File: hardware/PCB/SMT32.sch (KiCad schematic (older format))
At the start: 25 parts, among them J1 USB_B_Micro, SW1 SW_DIP_x01, SW2 SW_DIP_x01, U3 AZ1117CH-3.3, U4 STM32F303CCTx, Y1 X50328MSB2GI

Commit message: Use the correct Footprint
I think I can't do more things before the parts arrive and figure out what LED im going to use
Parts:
- removed U3: AZ1117CH-3.3, Package_TO_SOT_SMD:SOT-223-3_TabPin2, symbol Regulator_Linear:LD1117S33TR_SOT223
- added R14: 100k, Resistor_SMD:R_0402_1005Metric, symbol Device:R
- added U3: AZ1117-3.3, Package_TO_SOT_SMD:SOT-223-3_TabPin2, symbol Regulator_Linear:AZ1117-3.3
- renumbered C18 to C15, C17 to C16, C19 to C17, C20 to C18, C1 to C19, C22 to C20, C26 to C21, C23 to C22, C24 to C23, C25 to C24, R12 to R10, R13 to R11, R14 to R12, R15 to R13, R16 to R15, R17 to R16, R18 to R17, R19 to R18, R11 to R9
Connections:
- wire segments 65 -> 67
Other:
- moved on the sheet: R16

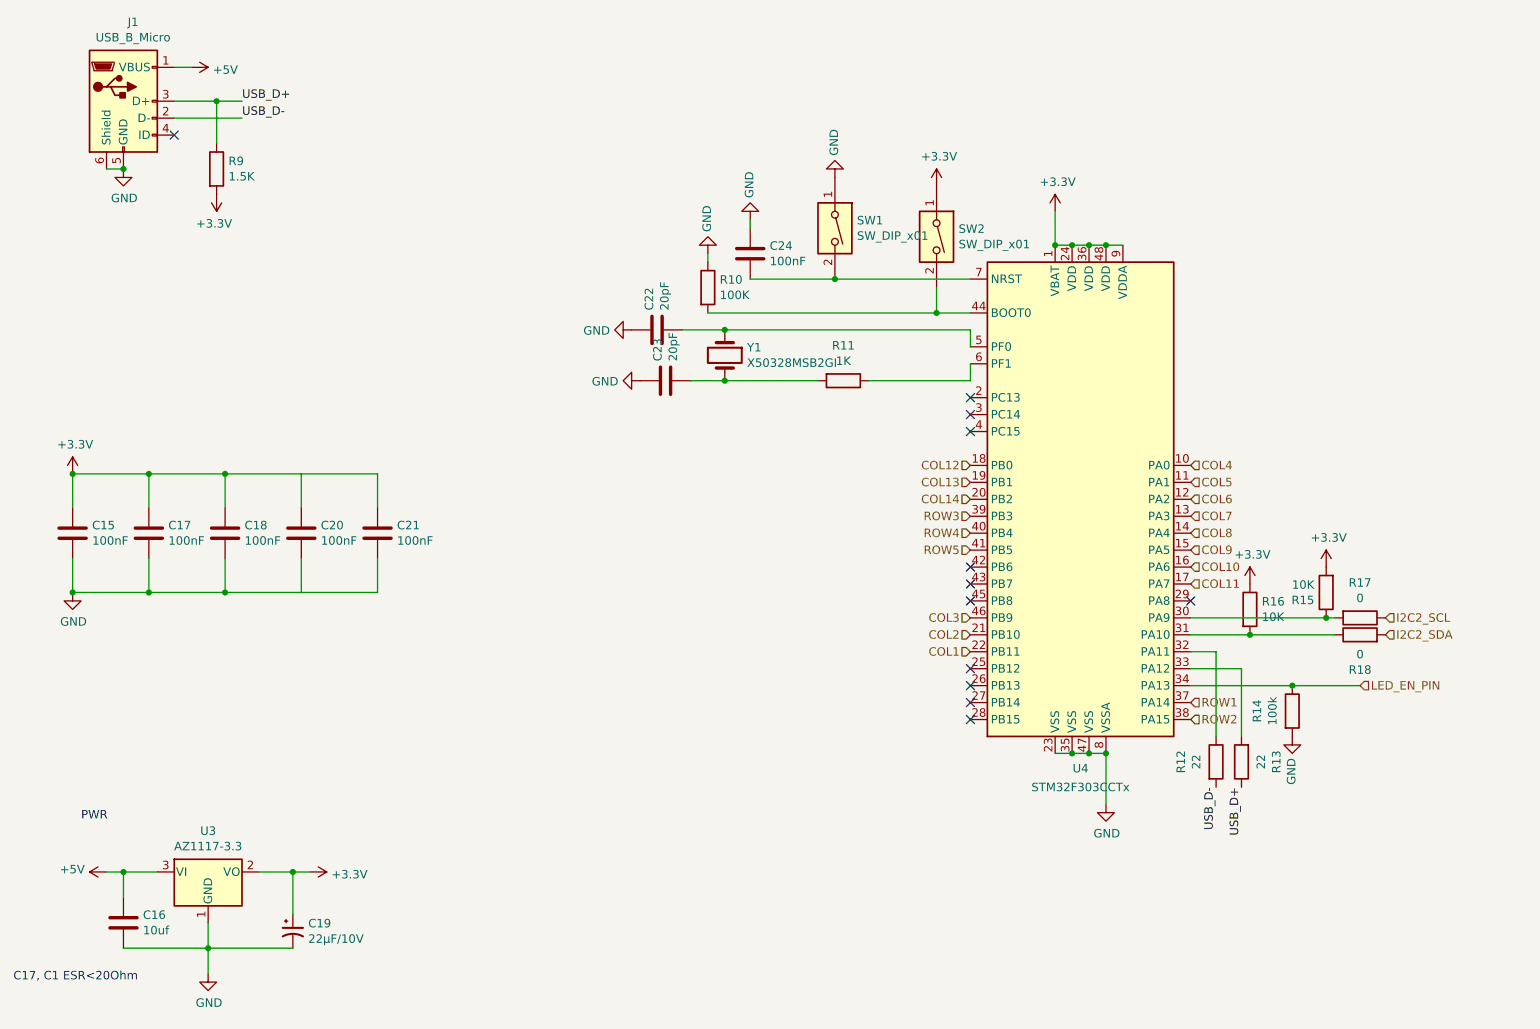
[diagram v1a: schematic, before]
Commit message: alot of changes
modify the QFN-48 so PCB 3d view in future would look better (so I don't design a part that doesn't fit)
I made a useless QFN-40 3d model
modify schematics so it looks better
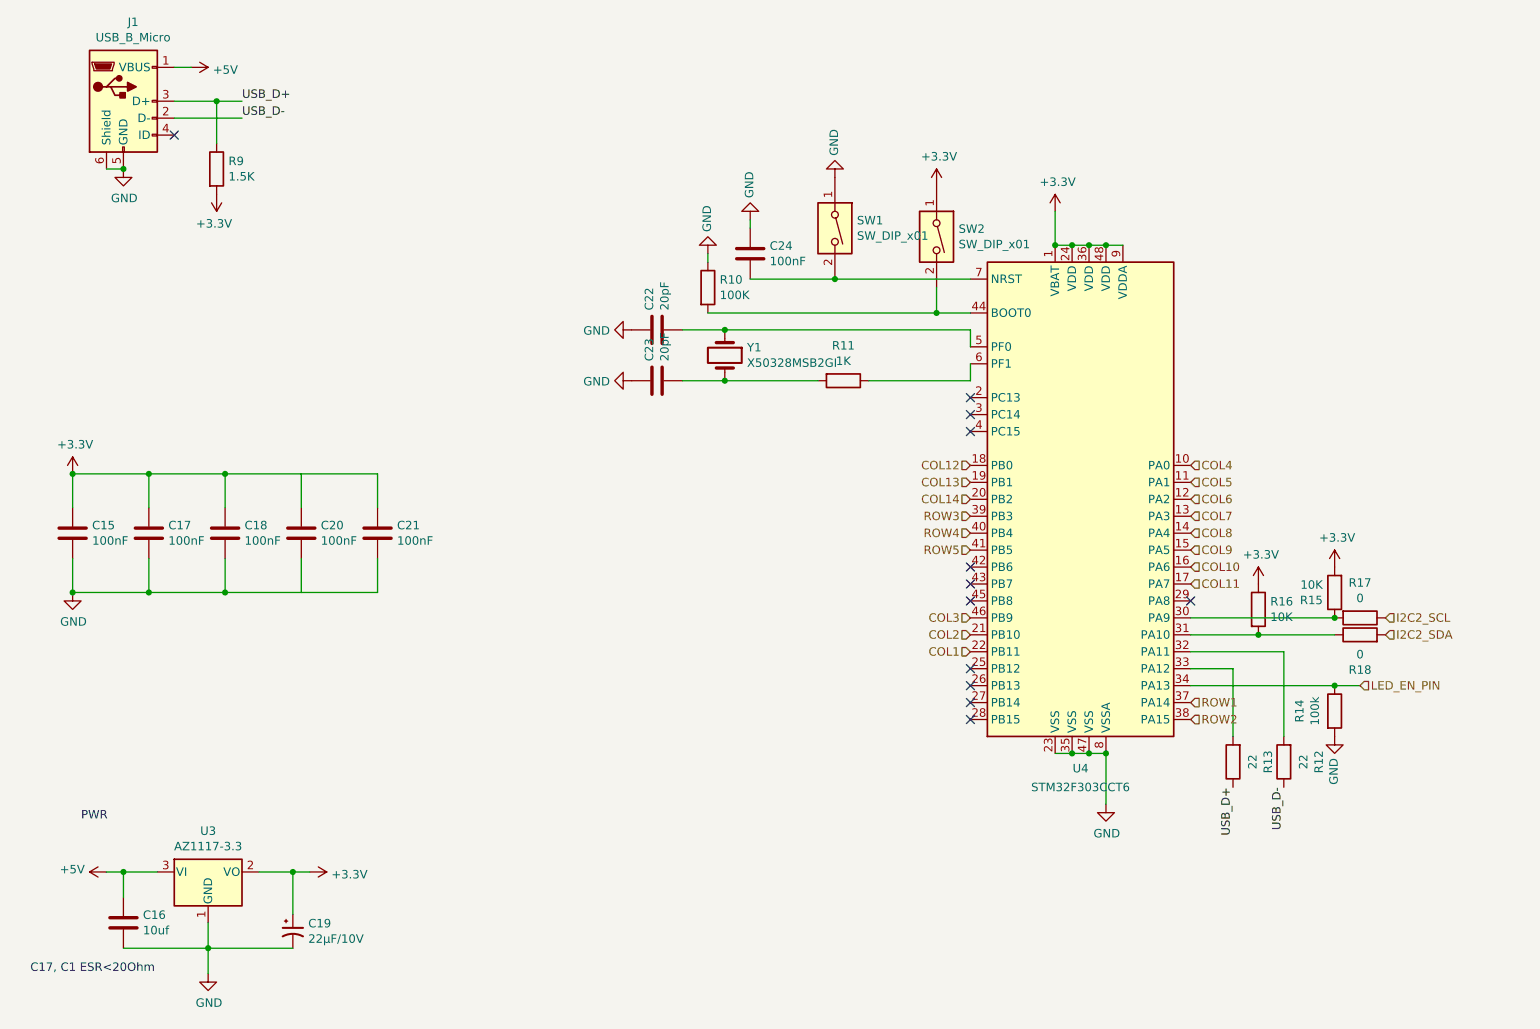
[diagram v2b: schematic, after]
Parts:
- C15, C17, C18, C20, C21, C24: Footprint (none) -> Capacitor_SMD:C_0402_1005Metric; Value (none) -> 100nf
- C16: Footprint (none) -> Capacitor_SMD:C_0402_1005Metric; Value (none) -> 10uf
- C22, C23: Footprint (none) -> Capacitor_SMD:C_0402_1005Metric; Value (none) -> 20pf
- R10: Footprint (none) -> Resistor_SMD:R_0402_1005Metric; Value (none) -> 100k
- R11: Footprint (none) -> Resistor_SMD:R_0402_1005Metric; Value (none) -> 1k
- R12, R13: Footprint (none) -> Resistor_SMD:R_0402_1005Metric; Value (none) -> 22
- R14: Footprint Resistor_SMD:R_0603_1608Metric_Pad1.05x0.95mm_HandSolder -> Resistor_SMD:R_0402_1005Metric
- R15, R16: Footprint (none) -> Resistor_SMD:R_0402_1005Metric; Value (none) -> 10k
- R17, R18: Footprint (none) -> Resistor_SMD:R_0402_1005Metric; Value (none) -> 0
- R9: Footprint (none) -> Resistor_SMD:R_0402_1005Metric; Value (none) -> 1.5k
- U3: Footprint (none) -> Package_TO_SOT_SMD:SOT-223-3_TabPin2; Value (none) -> AS1117-3.3
- U4: value STM32F303CCTx -> STM32F303CCT6; Footprint (none) -> Package_QFP:LQFP-48_7x7mm_P0.5mm; Value (none) -> STM32F303CCT6
- Y1: Footprint (none) -> Crystal:Crystal_SMD_5032-2Pin_5.0x3.2mm; Value (none) -> X50328MSB2GI
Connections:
- net USB_D-: now also R12.1; no longer R12.2
- net at U4.32 (PA11): now also R12.2; no longer R12.1
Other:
- moved on the sheet: C23, R12, R13, R14, R15, R16

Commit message: making progress
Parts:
- removed C19: 22μF/10V, Capacitor_Tantalum_SMD:CP_EIA-3216-18_Kemet-A, symbol Device:CP1_Small
- added C19: 22uf, Capacitor_SMD:C_0402_1005Metric, symbol Device:C
- J1: value USB_B_Micro -> 473460001; footprint Connector_USB:USB_Micro-B_Molex-105017-0001 -> Connector_USB:USB_Micro-B_Molex_47346-0001
- SW1, SW2: value SW_DIP_x01 -> B3U-1000P
- U3: value AZ1117-3.3 -> AZ1117CH-3.3TRG1
- Y1: value X50328MSB2GI -> 8Mhz20pF
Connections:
- net +3V3: now also C19.1
- net GND: now also C19.2
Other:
- note added: "8Mhz External Crystal\nChange CL capasitors when using different crystal"
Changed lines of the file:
@@
 P 5600 2250
 F 0 "SW1" V 5554 2380 50  0000 L CNN
-F 1 "SW_DIP_x01" V 5645 2380 50  0000 L CNN
+F 1 "B3U-1000P" V 5645 2380 50  0000 L CNN
 F 2 "Button_Switch_SMD:SW_SPST_B3U-1000P" H 5600 2250 50  0001 C CNN
 F 3 "~" H 5600 2250 50  0001 C CNN
@@
 P 6200 2300
 F 0 "SW2" V 6154 2430 50  0000 L CNN
-F 1 "SW_DIP_x01" V 6245 2430 50  0000 L CNN
+F 1 "B3U-1000P" V 6245 2430 50  0000 L CNN
 F 2 "Button_Switch_SMD:SW_SPST_B3U-1000P" H 6200 2300 50  0001 C CNN
 F 3 "~" H 6200 2300 50  0001 C CNN
@@
 P 1400 1500
 F 0 "J1" H 1457 1967 50  0000 C CNN
-F 1 "USB_B_Micro" H 1457 1876 50  0000 C CNN
-F 2 "Connector_USB:USB_Micro-B_Molex-105017-0001" H 1550 1450 50  0001 C CNN
+F 1 "473460001" H 1457 1876 50  0000 C CNN
+F 2 "Connector_USB:USB_Micro-B_Molex_47346-0001" H 1550 1450 50  0001 C CNN
 F 3 "~" H 1550 1450 50  0001 C CNN
 	1    1400 1500
@@
 P 4950 3000
 F 0 "Y1" V 4904 3131 50  0000 L CNN
-F 1 "X50328MSB2GI" V 4995 3131 50  0000 L CNN
+F 1 "8Mhz20pF" V 4995 3131 50  0000 L CNN
 F 2 "Crystal:Crystal_SMD_5032-2Pin_5.0x3.2mm" H 4950 3000 50  0001 C CNN
 F 3 "~" H 4950 3000 50  0001 C CNN
@@
 NoConn ~ 6400 5050
 Wire Wire Line
-	2200 6050 2400 6050
-Wire Wire Line
 	1300 6050 1400 6050
-Connection ~ 2400 6050
-Wire Wire Line
-	2400 6050 2500 6050
 Wire Wire Line
 	1400 6200 1400 6050
@@
 	1    0    0    -1
 $EndComp
-$Comp
-L Device:CP1_Small C?
-U 1 1 5E31A107
-P 2400 6400
-AR Path="/5EC33E3D/5E31A107" Ref="C?"  Part="1"
-AR Path="/5E1424B2/5E31A107" Ref="C19"  Part="1"
-F 0 "C19" H 2491 6446 50  0000 L CNN
-F 1 "22μF/10V" H 2491 6355 50  0000 L CNN
-F 2 "Capacitor_Tantalum_SMD:CP_EIA-3216-18_Kemet-A" H 2400 6400 50  0001 C CNN
-F 3 "~" H 2400 6400 50  0001 C CNN
-F 4 "Capacitor_Tantalum_SMD:CP_EIA-3528-12_Kemet-T_Pad1.50x2.35mm_HandSolder" H 2400 6400 50  0001 C CNN "Footprint"
-F 5 "22μF/10V" H 2400 6400 50  0001 C CNN "Value"
-	1    2400 6400
-	1    0    0    -1
-$EndComp
-Wire Wire Line
-	2400 6050 2400 6300
 Text Notes 850  6650 0    50   ~ 0
 C17, C1 ESR<20Ohm
@@
 P 1900 6050
 F 0 "U3" H 1900 6292 50  0000 C CNN
-F 1 "AZ1117-3.3" H 1900 6201 50  0000 C CNN
+F 1 "AZ1117CH-3.3TRG1" H 1900 6201 50  0000 C CNN
 F 2 "Package_TO_SOT_SMD:SOT-223-3_TabPin2" H 1900 6300 50  0001 C CIN
 F 3 "https://www.diodes.com/assets/Datasheets/AZ1117.pdf" H 1900 6050 50  0001 C CNN
@@
 Wire Wire Line
 	8250 4750 8250 5250
+$Comp
+L Device:C C19
+U 1 1 5E352E15
+P 2400 6350
+F 0 "C19" H 2515 6396 50  0000 L CNN
+F 1 "22uf" H 2515 6305 50  0000 L CNN
+F 2 "Capacitor_SMD:C_0402_1005Metric" H 2438 6200 50  0001 C CNN
+F 3 "~" H 2400 6350 50  0001 C CNN
+F 4 "Capacitor_SMD:C_0402_1005Metric" H 2400 6350 50  0001 C CNN "Footprint"
+F 5 "10uf" H 2400 6350 50  0001 C CNN "Value"
+	1    2400 6350
+	1    0    0    -1
+$EndComp
+Wire Wire Line
+	2200 6050 2400 6050
+Wire Wire Line
+	2400 6200 2400 6050
+Connection ~ 2400 6050
+Wire Wire Line
+	2400 6050 2500 6050
+Text Notes 4300 3550 0    50   ~ 0
+8Mhz External Crystal\nChange CL capasitors when using different crystal
 $EndSCHEMATC

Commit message: Make it nicer, rev0.1 alpha
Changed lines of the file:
@@
 Sheet 6 6
 Title "NHW68"
-Date "2020-01-28"
+Date "2020-01-31"
 Rev "0.1"
 Comp ""
@@
 Wire Wire Line
 	2400 6050 2500 6050
-Text Notes 4300 3550 0    50   ~ 0
+Text Notes 4150 3450 0    50   ~ 0
 8Mhz External Crystal\nChange CL capasitors when using different crystal
 $EndSCHEMATC

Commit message: attempt to remove some extra values
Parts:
- C15, C17, C18, C20, C21, C24: Footprint Capacitor_SMD:C_0402_1005Metric -> (none); Value 100nf -> (none)
- C16, C19: Footprint Capacitor_SMD:C_0402_1005Metric -> (none); Value 10uf -> (none)
- C22, C23: Footprint Capacitor_SMD:C_0402_1005Metric -> (none); Value 20pf -> (none)
- R10, R14: Footprint Resistor_SMD:R_0402_1005Metric -> (none); Value 100k -> (none)
- R11: Footprint Resistor_SMD:R_0402_1005Metric -> (none); Value 1k -> (none)
- R12, R13: Footprint Resistor_SMD:R_0402_1005Metric -> (none); Value 22 -> (none)
- R15, R16: Footprint Resistor_SMD:R_0402_1005Metric -> (none); Value 10k -> (none)
- R17, R18: Footprint Resistor_SMD:R_0402_1005Metric -> (none); Value 0 -> (none)
- R9: Footprint Resistor_SMD:R_0402_1005Metric -> (none); Value 1.5k -> (none)
- U3: Footprint Package_TO_SOT_SMD:SOT-223-3_TabPin2 -> (none); Value AS1117-3.3 -> (none)
- U4: Footprint Package_QFP:LQFP-48_7x7mm_P0.5mm -> (none); Value STM32F303CCT6 -> (none)
- Y1: Footprint Crystal:Crystal_SMD_5032-2Pin_5.0x3.2mm -> (none); P/N (none) -> X50328MSB2GI; Value X50328MSB2GI -> (none)

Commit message: add in part number so I could use it for the bom
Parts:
- J1: Part Number (none) -> 47346-0001
- SW1, SW2: Part Number (none) -> B3U-1000P
- U3: Part Number (none) -> AZ1117CH-3.3TRG1
- U4: Part Number (none) -> STM32F303CCT6
- Y1: P/N X50328MSB2GI -> (none); Part Number (none) -> X50328MSB2GI
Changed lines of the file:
@@
 F 2 "Package_TO_SOT_SMD:SOT-223-3_TabPin2" H 1900 6300 50  0001 C CIN
 F 3 "https://www.diodes.com/assets/Datasheets/AZ1117.pdf" H 1900 6050 50  0001 C CNN
+F 4 "AZ1117CH-3.3TRG1" H 1900 6050 50  0001 C CNN "Part Number"
 	1    1900 6050
 	1    0    0    -1
@@
 F 2 "Crystal:Crystal_SMD_5032-2Pin_5.0x3.2mm" H 4950 3000 50  0001 C CNN
 F 3 "~" H 4950 3000 50  0001 C CNN
-F 4 "X50328MSB2GI" V 4950 3000 50  0001 C CNN "P/N"
+F 4 "X50328MSB2GI" H 4950 3000 50  0001 C CNN "Part Number"
 	1    4950 3000
 	0    1    1    0
@@
 F 1 "473460001" H 1457 1876 50  0000 C CNN
 F 2 "Connector_USB:USB_Micro-B_Molex_47346-0001" H 1550 1450 50  0001 C CNN
-F 3 "~" H 1550 1450 50  0001 C CNN
+F 3 "https://www.molex.com/pdm_docs/ps/PS-47346-001-001.pdf" H 1550 1450 50  0001 C CNN
+F 4 "47346-0001" H 1400 1500 50  0001 C CNN "Part Number"
 	1    1400 1500
 	1    0    0    -1
@@
 F 1 "B3U-1000P" V 6245 2430 50  0000 L CNN
 F 2 "Button_Switch_SMD:SW_SPST_B3U-1000P" H 6200 2300 50  0001 C CNN
-F 3 "~" H 6200 2300 50  0001 C CNN
+F 3 "https://omronfs.omron.com/en_US/ecb/products/pdf/en-b3u.pdf" H 6200 2300 50  0001 C CNN
+F 4 "B3U-1000P" H 6200 2300 50  0001 C CNN "Part Number"
 	1    6200 2300
 	0    1    1    0
@@
 F 1 "B3U-1000P" V 5645 2380 50  0000 L CNN
 F 2 "Button_Switch_SMD:SW_SPST_B3U-1000P" H 5600 2250 50  0001 C CNN
-F 3 "~" H 5600 2250 50  0001 C CNN
+F 3 "https://omronfs.omron.com/en_US/ecb/products/pdf/en-b3u.pdf" H 5600 2250 50  0001 C CNN
+F 4 "B3U-1000P" H 5600 2250 50  0001 C CNN "Part Number"
 	1    5600 2250
 	0    1    1    0
@@
 F 2 "Package_QFP:LQFP-48_7x7mm_P0.5mm" H 6500 2450 50  0001 R CNN
 F 3 "http://www.st.com/st-web-ui/static/active/en/resource/technical/document/datasheet/DM00058181.pdf" H 7100 3850 50  0001 C CNN
+F 4 "STM32F303CCT6" H 7100 3850 50  0001 C CNN "Part Number"
 	1    7100 3850
 	1    0    0    -1
